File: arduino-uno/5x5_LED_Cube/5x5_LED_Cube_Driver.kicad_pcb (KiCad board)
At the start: 2 copper layers, 88.9 x 81.3 mm, 42 parts, among them J1 Arduino, J2 Power, J3 Layers, Q1 DMG2305UX, Q2 DMG2305UX, Q3 DMG2305UX, Q4 DMG2305UX, Q5 DMG2305UX, U1 TLC5940NT, U2 TLC5940NT

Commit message: Replaced the SIP resistor with SMD ones
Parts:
- removed RN1: 4.7K, Resistor_THT:R_Array_SIP6
- added R4: 4.7K, Resistor_SMD:R_0603_1608Metric, F.Cu at (158.0, 123.2)
- added R5: 4.7K, Resistor_SMD:R_0603_1608Metric, F.Cu at (158.0, 125.7)
- added R6: 4.7K, Resistor_SMD:R_0603_1608Metric, F.Cu at (158.0, 128.3)
- added R7: 4.7K, Resistor_SMD:R_0603_1608Metric, F.Cu at (158.0, 130.8)
- added R8: 4.7K, Resistor_SMD:R_0603_1608Metric, F.Cu at (158.0, 133.3)
- moved Q1 1.83 mm to (119.4, 134.3)
- moved Q2 1.83 mm to (127.0, 134.3)
- moved Q3 1.83 mm to (134.6, 134.3)
- moved Q4 1.83 mm to (142.2, 134.3)
- moved D10 1.83 mm to (154.4, 77.2)
- moved D11 1.83 mm to (97.2, 91.5)
- moved D12 1.83 mm to (111.5, 91.5)
- moved D13 1.83 mm to (125.8, 91.5)
- moved D14 1.83 mm to (140.1, 91.5)
- moved D15 1.83 mm to (154.4, 91.5)
- moved D6 1.83 mm to (97.2, 77.2)
- moved D7 1.83 mm to (111.5, 77.2)
- moved D8 1.83 mm to (125.8, 77.2)
- moved D9 1.83 mm to (140.1, 77.2)
- moved J1 1.83 mm to (180.3, 95.2)
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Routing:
- net +5V: track 177.2 -> 190.7 mm
- net /Layer5Gate: track 19.4 -> 21.9 mm, vias 1 -> 2
- net /Layer1Gate: track 54.1 -> 56.6 mm, vias 1 -> 2
- net /Layer3Gate: track 36.7 -> 39.3 mm, vias 1 -> 2
- net /Layer2Gate: track 45.4 -> 47.9 mm, vias 1 -> 2
- net /Layer4Gate: track 28.0 -> 30.6 mm, vias 1 -> 2

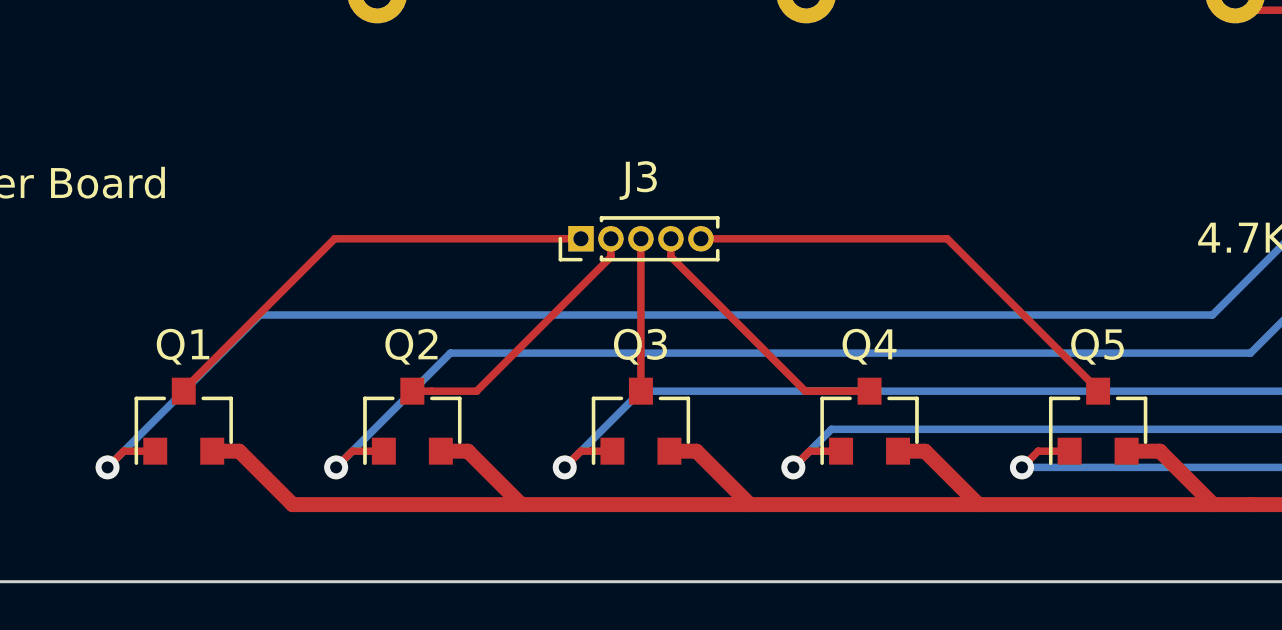
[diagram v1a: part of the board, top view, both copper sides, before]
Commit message: Grouped the PCB traces for layers closer together
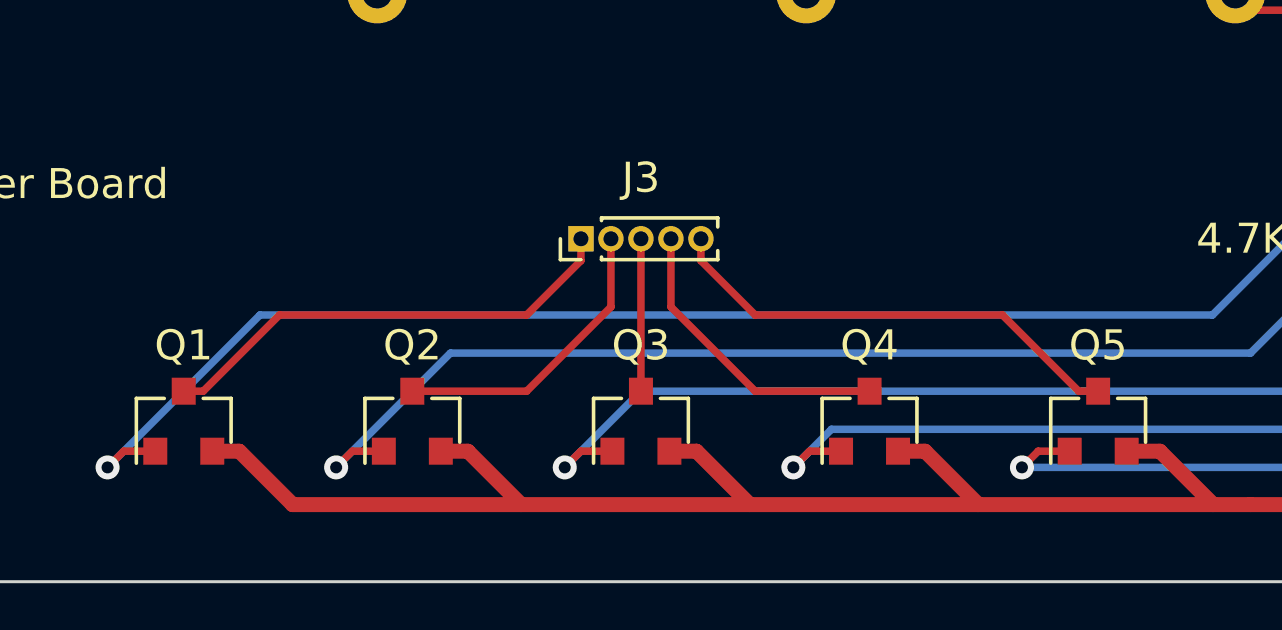
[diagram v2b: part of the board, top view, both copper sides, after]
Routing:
- net /Layer4: track 9.08 -> 10.1 mm
- net /Layer2: track 9.08 -> 10.1 mm
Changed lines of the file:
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@@
     (thickness 1.6)
     (drawings 23)
-    (tracks 236)
+    (tracks 238)
     (zones 0)
     (modules 46)
@@
     (add_net /SOUT1)
     (add_net GND)
-    (add_net "Net-(U1-Pad16)")
-    (add_net "Net-(U2-Pad14)")
-    (add_net "Net-(U2-Pad15)")
-    (add_net "Net-(U2-Pad16)")
-    (add_net "Net-(U2-Pad17)")
   )
   (module Resistor_SMD:R_0603_1608Metric (layer F.Cu)
@@
   (segment (start 180.34 107.68) (end 181.34 107.68) (width 0.5) (layer B.Cu) (net 2))
   (segment (start 180.34 107.68) (end 181.594 107.68) (width 0.5) (layer F.Cu) (net 2))
-  (segment (start 149.86 133.3) (end 149.86 133.35) (width 0.25) (layer F.Cu) (net 3))
-  (segment (start 144.83 128.27) (end 149.86 133.3) (width 0.25) (layer F.Cu) (net 3))
-  (segment (start 136.62 128.27) (end 144.83 128.27) (width 0.25) (layer F.Cu) (net 3))
-  (segment (start 141.59 133.35) (end 142.24 133.35) (width 0.25) (layer F.Cu) (net 4))
-  (segment (start 140.09896 133.35) (end 141.59 133.35) (width 0.25) (layer F.Cu) (net 4))
-  (segment (start 135.62 128.87104) (end 140.09896 133.35) (width 0.25) (layer F.Cu) (net 4))
-  (segment (start 135.62 128.27) (end 135.62 128.87104) (width 0.25) (layer F.Cu) (net 4))
+  (segment (start 149.21 133.35) (end 146.67 130.81) (width 0.25) (layer F.Cu) (net 3))
+  (segment (start 149.86 133.35) (end 149.21 133.35) (width 0.25) (layer F.Cu) (net 3))
+  (segment (start 136.62 128.27) (end 136.62 129) (width 0.25) (layer F.Cu) (net 3))
+  (segment (start 138.43 130.81) (end 146.67 130.81) (width 0.25) (layer F.Cu) (net 3))
+  (segment (start 136.62 129) (end 138.43 130.81) (width 0.25) (layer F.Cu) (net 3))
+  (segment (start 135.62 128.27) (end 135.62 130.54) (width 0.25) (layer F.Cu) (net 4))
+  (segment (start 138.43 133.35) (end 142.24 133.35) (width 0.25) (layer F.Cu) (net 4))
+  (segment (start 135.62 130.54) (end 138.43 133.35) (width 0.25) (layer F.Cu) (net 4))
   (segment (start 134.62 133.35) (end 134.62 128.27) (width 0.25) (layer F.Cu) (net 5))
-  (segment (start 127.65 133.35) (end 127 133.35) (width 0.25) (layer F.Cu) (net 6))
-  (segment (start 129.14104 133.35) (end 127.65 133.35) (width 0.25) (layer F.Cu) (net 6))
-  (segment (start 133.62 128.87104) (end 129.14104 133.35) (width 0.25) (layer F.Cu) (net 6))
-  (segment (start 133.62 128.27) (end 133.62 128.87104) (width 0.25) (layer F.Cu) (net 6))
-  (segment (start 119.38 133.3) (end 119.38 133.35) (width 0.25) (layer F.Cu) (net 7))
-  (segment (start 124.41 128.27) (end 119.38 133.3) (width 0.25) (layer F.Cu) (net 7))
-  (segment (start 132.62 128.27) (end 124.41 128.27) (width 0.25) (layer F.Cu) (net 7))
+  (segment (start 133.62 128.27) (end 133.62 130.54) (width 0.25) (layer F.Cu) (net 6))
+  (segment (start 130.81 133.35) (end 127 133.35) (width 0.25) (layer F.Cu) (net 6))
+  (segment (start 133.62 130.54) (end 130.81 133.35) (width 0.25) (layer F.Cu) (net 6))
+  (segment (start 132.62 128.27) (end 132.62 129) (width 0.25) (layer F.Cu) (net 7))
+  (segment (start 132.62 129) (end 130.81 130.81) (width 0.25) (layer F.Cu) (net 7))
+  (segment (start 120.03 133.35) (end 119.38 133.35) (width 0.25) (layer F.Cu) (net 7))
+  (segment (start 122.57 130.81) (end 120.03 133.35) (width 0.25) (layer F.Cu) (net 7))
+  (segment (start 130.81 130.81) (end 122.57 130.81) (width 0.25) (layer F.Cu) (net 7))
   (segment (start 118.43 135.35) (end 117.38 135.35) (width 0.25) (layer F.Cu) (net 8))
   (segment (start 117.38 135.35) (end 116.84 135.89) (width 0.25) (layer F.Cu) (net 8))

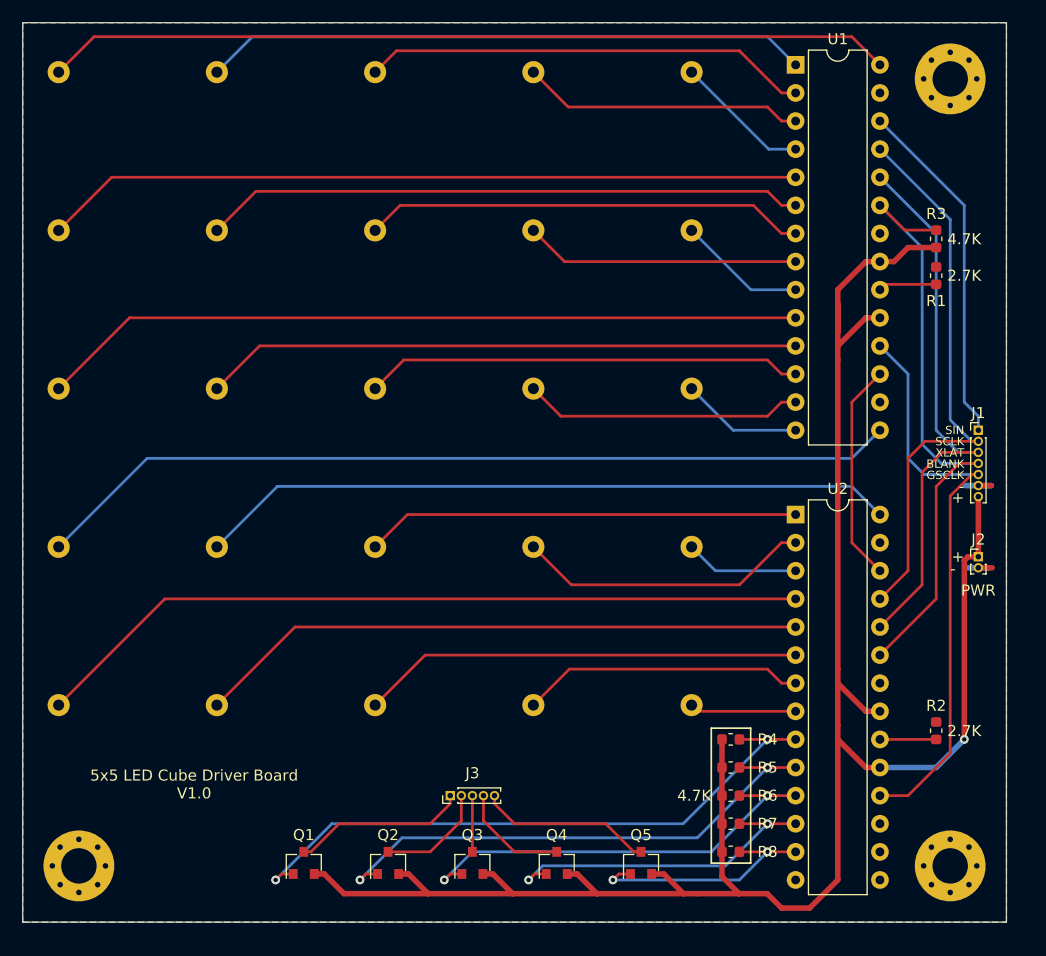
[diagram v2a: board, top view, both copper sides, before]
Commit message: Fixed the headers being too small for the wires
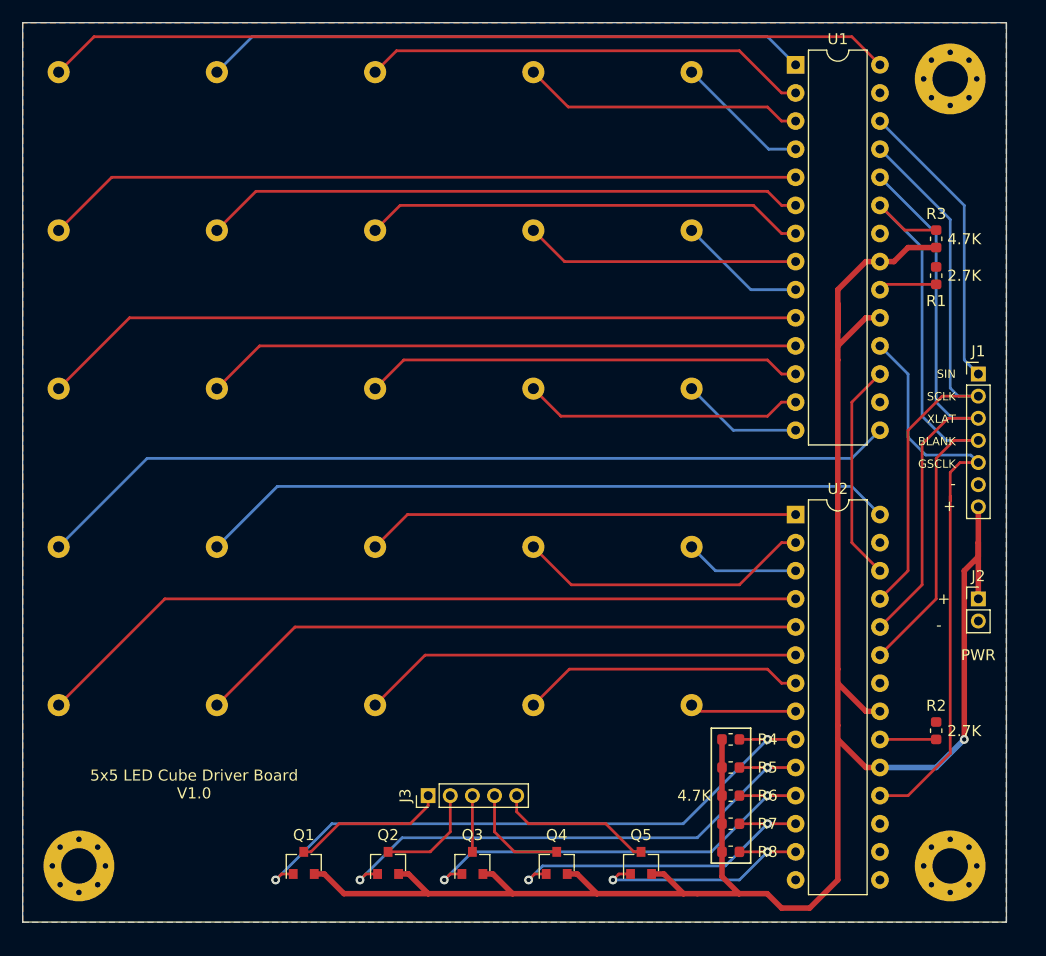
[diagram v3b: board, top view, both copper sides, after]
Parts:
- J1: footprint Connector_PinHeader_1.00mm:PinHeader_1x07_P1.00mm_Vertical -> Connector_PinHeader_2.00mm:PinHeader_1x07_P2.00mm_Vertical
- J2: footprint Connector_PinHeader_1.00mm:PinHeader_1x02_P1.00mm_Vertical -> Connector_PinHeader_2.00mm:PinHeader_1x02_P2.00mm_Vertical
- J3: footprint Connector_PinHeader_1.00mm:PinHeader_1x05_P1.00mm_Vertical -> Connector_PinHeader_2.00mm:PinHeader_1x05_P2.00mm_Vertical
- moved J1 5.08 mm to (180.3, 90.2)
- moved J2 3.81 mm to (180.3, 110.5)
- moved J3 2.00 mm to (130.6, 128.3)
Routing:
- net GND: track 6.82 -> 0.00 mm
- net /ArduinoD11(SIN): track 31.6 -> 26.5 mm
- net +5V: track 190.7 -> 194.3 mm
- net /Layer1: track 15.8 -> 13.9 mm
- net /Layer5: track 15.8 -> 14.2 mm
